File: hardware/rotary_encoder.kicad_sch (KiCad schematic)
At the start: 7 parts, among them U14 PEC11R-4215F-S0024

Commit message: Minor cosmetic changes
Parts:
- U14: footprint TO_215F-S0024 -> kitchen_timer:TO_215F-S0024
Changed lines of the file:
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@@
 			)
 		)
-		(property "Footprint" "TO_215F-S0024"
+		(property "Footprint" "kitchen_timer:TO_215F-S0024"
 			(at 102.108 72.39 0)
 			(effects

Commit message: Added information, footprints and 3d models for several components
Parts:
- U14: Package (none) -> Through_Hole; Part Num (none) -> PEC11R-4215F-S0024; Price/unit (none) -> $2.4720; Supplier Link (none) -> https://jlcpcb.com/partdetail/Bourns-PEC11R_4215FS0024/C143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
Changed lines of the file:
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@@
 			)
 		)
-		(property "Datasheet" "PEC11R-4215F-S0024"
+		(property "Datasheet" "https://www.lcsc.com/datasheet/lcsc_datasheet_2304140030_BOURNS-PEC11R-4215F-S0024_C143790.pdf"
 			(at 98.806 69.85 0)
 			(effects
@@
 			)
 		)
-		(property "Description" ""
+		(property "Description" "Plugin Rotary Encoders ROHS"
 			(at 123.19 73.66 90)
 			(effects
 				(font
+					(size 1.27 1.27)
+				)
+				(hide yes)
+			)
+		)
+		(property "Supplier Link" "https://jlcpcb.com/partdetail/Bourns-PEC11R_4215FS0024/C143790"
+			(at 124.46 80.01 0)
+			(effects
+				(font
+					(size 1.27 1.27)
+				)
+				(hide yes)
+			)
+		)
+		(property "Price/unit" "$2.4720"
+			(at 124.46 80.01 0)
+			(effects
+				(font
+					(size 1.27 1.27)
+				)
+				(hide yes)
+			)
+		)
+		(property "Part Num" "PEC11R-4215F-S0024"
+			(at 124.46 80.01 0)
+			(effects
+				(font
+					(size 1.27 1.27)
+				)
+				(hide yes)
+			)
+		)
+		(property "Package" "Through_Hole"
+			(at 124.46 80.01 0)
+			(effects
+				(font

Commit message: Added 3d models for footprints
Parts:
- U14: footprint kitchen_timer:TO_215F-S0024 -> kitchen_timer:PEC11R4215FS0024
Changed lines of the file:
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@@
 			)
 		)
-		(property "Footprint" "kitchen_timer:TO_215F-S0024"
+		(property "Footprint" "kitchen_timer:PEC11R4215FS0024"
 			(at 102.108 72.39 0)
 			(effects

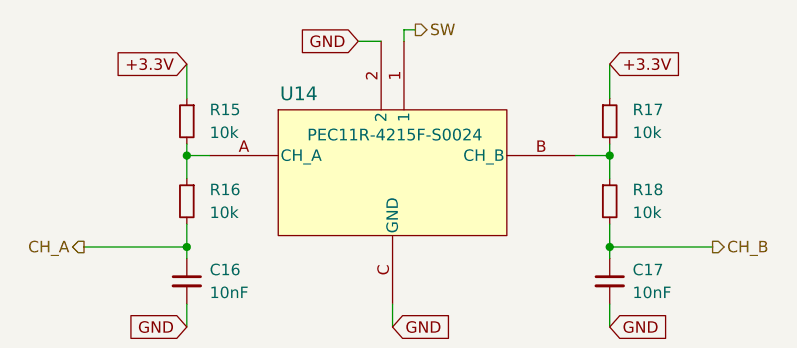
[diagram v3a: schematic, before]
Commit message: Removed the 3.3V Regulator since we might need to run everything out of 5V
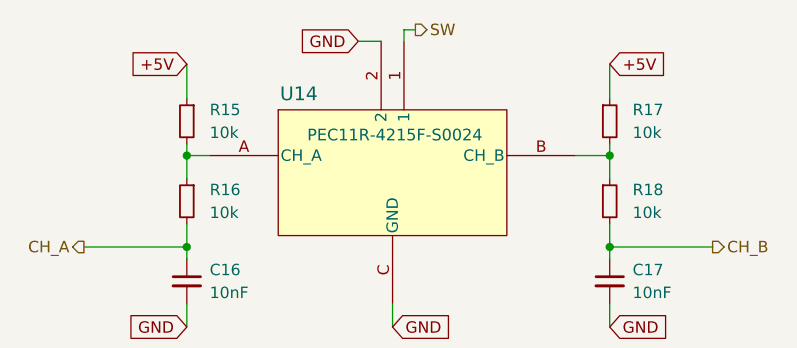
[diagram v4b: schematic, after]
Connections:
- net +3.3V renamed +5V
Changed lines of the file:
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@@
 		)
 	)
-	(global_label "+3.3V"
+	(global_label "+5V"
 		(shape input)
 		(at 101.6 68.58 180)
@@
 		)
 		(property "Intersheetrefs" "${INTERSHEET_REFS}"
-			(at 92.93 68.58 0)
+			(at 94.7443 68.58 0)
 			(effects
 				(font
@@
 		)
 	)
-	(global_label "+3.3V"
+	(global_label "+5V"
 		(shape input)
 		(at 148.59 68.58 0)
@@
 		)
 		(property "Intersheetrefs" "${INTERSHEET_REFS}"
-			(at 157.26 68.58 0)
+			(at 155.4457 68.58 0)
 			(effects
 				(font

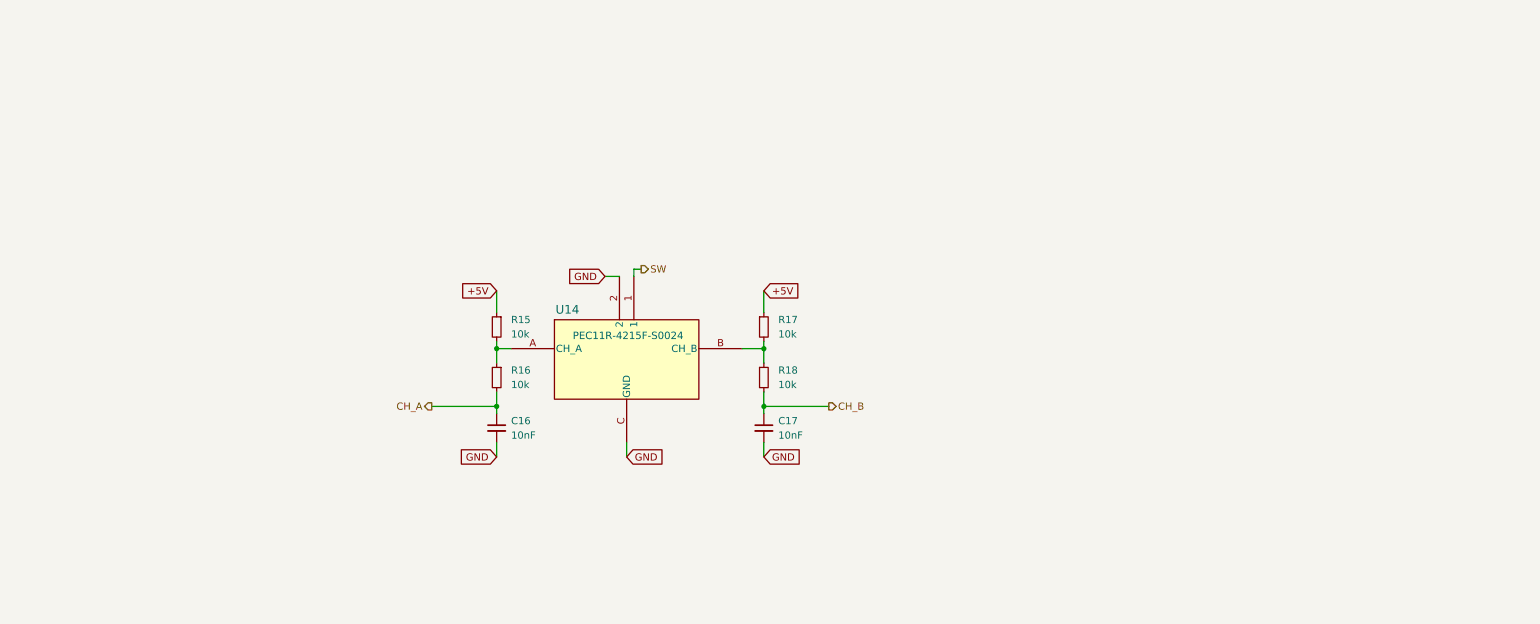
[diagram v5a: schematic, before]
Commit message: Schematic completed, commented and ready for review
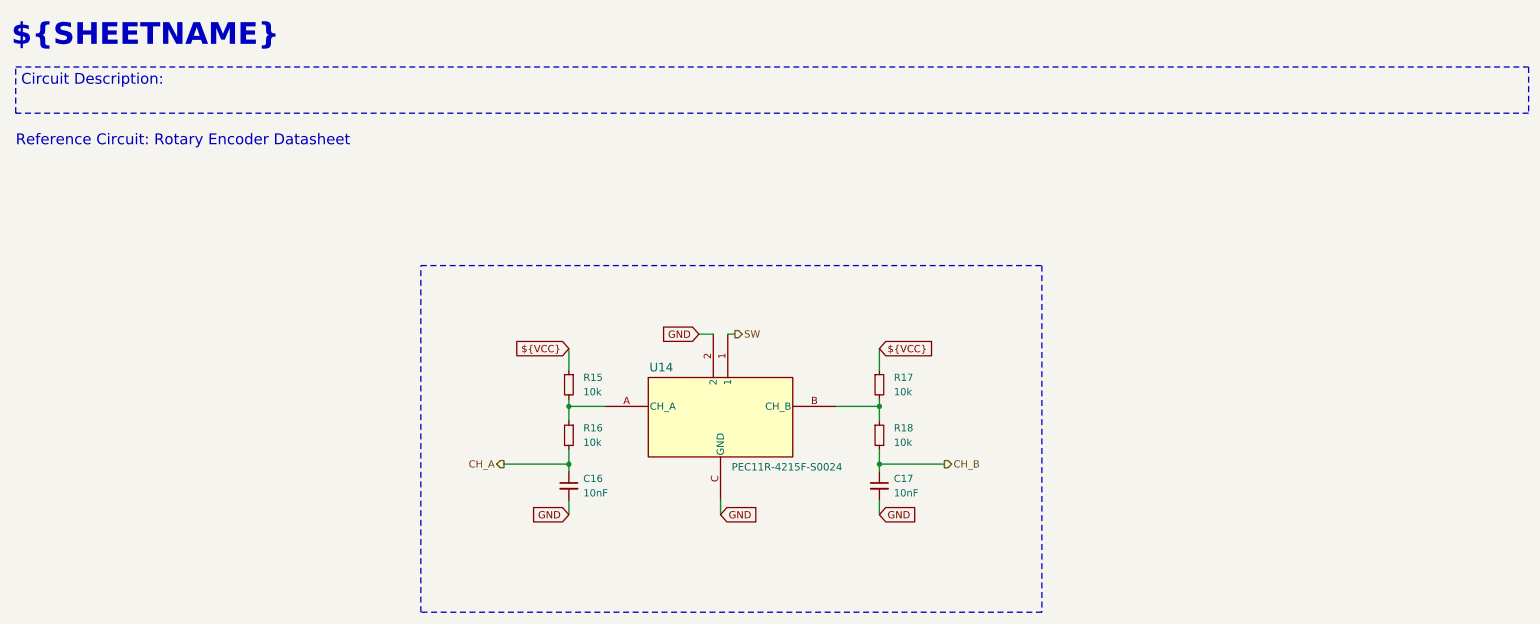
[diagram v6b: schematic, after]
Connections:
- net +5V renamed ${VCC}
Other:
- note added: "${SHEETNAME}"
- note added: "Reference Circuit: Rotary Encoder Datasheet"
- title: (none) -> Kitchen_Timer - ${SHEETNAME}
- moved on the sheet: C16, C17, R15, R16, R17, R18, U14

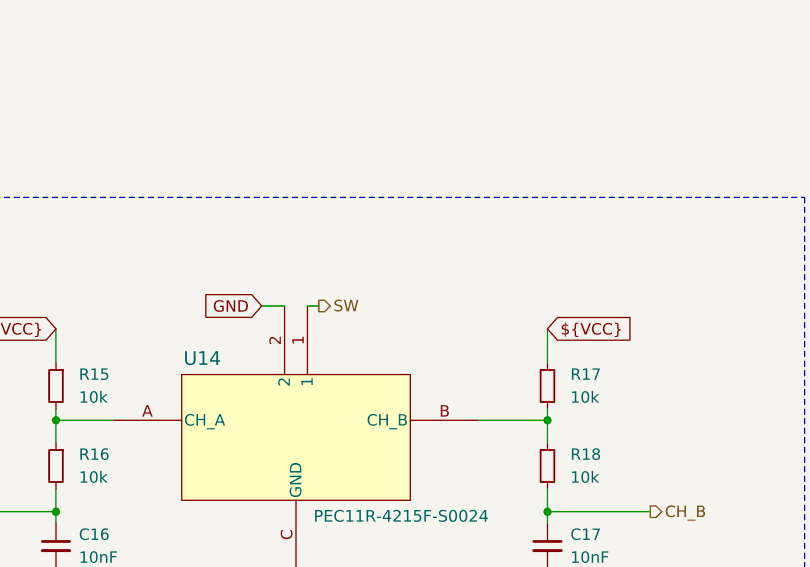
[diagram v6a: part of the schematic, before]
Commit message: Added filter to SW pin on Rotary Encoder
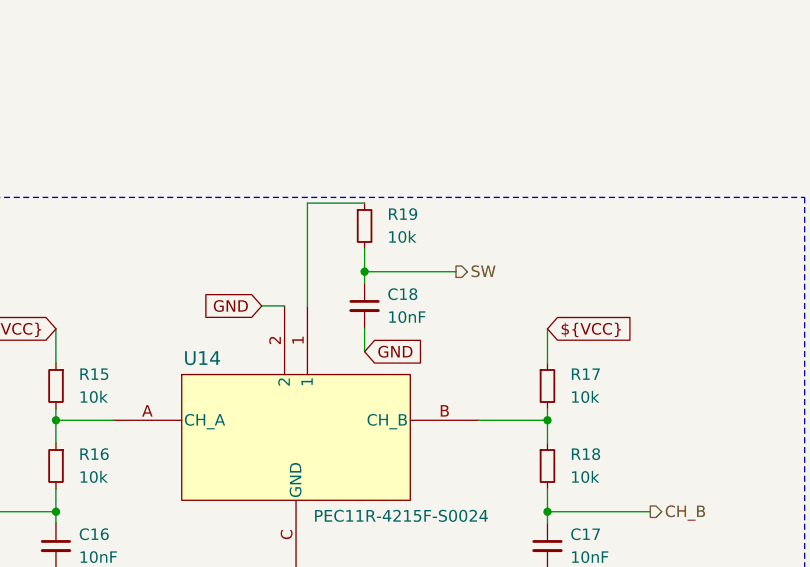
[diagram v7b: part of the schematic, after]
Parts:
- added C18: 10nF, symbol Device:C_Small
- added R19: 10k, symbol Device:R_Small
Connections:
- net GND: now also C18.2
- net SW: now also C18.1, R19.2; no longer U14.1
- new net: R19.1, U14.1
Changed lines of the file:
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@@
+	)
+	(junction
+		(at 148.59 72.39)
+		(diameter 0)
+		(color 0 0 0 0)
 	)
 	(junction
@@
 	(wire
 		(pts
-			(xy 143.51 76.2) (xy 142.24 76.2)
+			(xy 148.59 72.39) (xy 148.59 73.66)
 		)
 		(stroke
@@
 	(wire
 		(pts
+			(xy 148.59 72.39) (xy 158.75 72.39)
+		)
+		(stroke
+			(width 0)
+			(type default)
+		)
+	)
+	(wire
+		(pts
+			(xy 148.59 78.74) (xy 148.59 81.28)
+		)
+		(stroke
+			(width 0)
+			(type default)
+		)
+	)
+	(wire
+		(pts
 			(xy 114.3 88.9) (xy 114.3 87.63)
+		)
+		(stroke
+			(width 0)
+			(type default)
+		)
+	)
+	(wire
+		(pts
+			(xy 142.24 64.77) (xy 142.24 76.2)
+		)
+		(stroke
+			(width 0)
+			(type default)
+		)
+	)
+	(wire
+		(pts
+			(xy 142.24 64.77) (xy 148.59 64.77)
+		)
+		(stroke
+			(width 0)
+			(type default)
+		)
+	)
+	(wire
+		(pts
+			(xy 148.59 69.85) (xy 148.59 72.39)
 		)
 		(stroke
@@
 		)
 	)
+	(global_label "GND"
+		(shape input)
+		(at 148.59 81.28 0)
+		(fields_autoplaced yes)
+		(effects
+			(font
+				(size 1.27 1.27)
+			)
+			(justify left)
+		)
+		(property "Intersheetrefs" "${INTERSHEET_REFS}"
+			(at 155.4457 81.28 0)
+			(effects
+				(font
+					(size 1.27 1.27)
+				)
+				(justify left)
+				(hide yes)
+			)
+		)
+	)
 	(global_label "${VCC}"
 		(shape input)
@@
 	(hierarchical_label "SW"
 		(shape output)
-		(at 143.51 76.2 0)
+		(at 158.75 72.39 0)
 		(effects
 			(font
@@
 	(symbol
 		(lib_id "Device:R_Small")
+		(at 148.59 67.31 0)
+		(unit 1)
+		(exclude_from_sim no)
+		(in_bom yes)
+		(on_board yes)
+		(dnp no)
+		(fields_autoplaced yes)
+		(property "Reference" "R19"
+			(at 151.13 66.0399 0)
+			(effects
+				(font
+					(size 1.27 1.27)
+				)
+				(justify left)
+			)
+		)
+		(property "Value" "10k"
+			(at 151.13 68.5799 0)
+			(effects
+				(font
+					(size 1.27 1.27)
+				)
+				(justify left)
+			)
+		)
+		(property "Footprint" ""
+			(at 148.59 67.31 0)
+			(effects
+				(font
+					(size 1.27 1.27)
+				)
+				(hide yes)
+			)
+		)
+		(property "Datasheet" "~"
+			(at 148.59 67.31 0)
+			(effects
+				(font
+					(size 1.27 1.27)
+				)
+				(hide yes)
+			)
+		)
+		(property "Description" "Resistor, small symbol"
+			(at 148.59 67.31 0)
+			(effects
+				(font
+					(size 1.27 1.27)
+				)
+				(hide yes)
+			)
+		)
+		(pin "1"
+		)
+		(pin "2"
+		)
+		(instances
+			(project "kitchen_timer-hardware"
+				(path "/8963deea-96bc-4401-b671-98fbe9ed9c6a/0bd8e23b-f1a8-43a7-9e7f-c29366033bda"
+					(reference "R19")
+					(unit 1)
+				)
+			)
+		)
+	)
+	(symbol
+		(lib_id "Device:R_Small")
 		(at 114.3 85.09 0)
 		(mirror y)
@@
 					(unit 1)
 				)
+			)
+		)
+	)
+	(symbol
+		(lib_id "Device:C_Small")
+		(at 148.59 76.2 0)
+		(unit 1)
+		(exclude_from_sim no)
+		(in_bom yes)
+		(on_board yes)
+		(dnp no)
+		(fields_autoplaced yes)
+		(property "Reference" "C18"
+			(at 151.13 74.9362 0)
+			(effects
+				(font
+					(size 1.27 1.27)
+				)
+				(justify left)
+			)
+		)
+		(property "Value" "10nF"
+			(at 151.13 77.4762 0)
+			(effects
+				(font
+					(size 1.27 1.27)
+				)
+				(justify left)
+			)
+		)
+		(property "Footprint" ""
+			(at 148.59 76.2 0)
+			(effects
+				(font
+					(size 1.27 1.27)
+				)
+				(hide yes)
+			)
+		)
+		(property "Datasheet" "~"
+			(at 148.59 76.2 0)
+			(effects
+				(font
+					(size 1.27 1.27)
+				)
+				(hide yes)
+			)
+		)
+		(property "Description" "Unpolarized capacitor, small symbol"
+			(at 148.59 76.2 0)
+			(effects
+				(font
+					(size 1.27 1.27)
+				)
+				(hide yes)
+			)
+		)
+		(pin "1"
+		)
+		(pin "2"
+		)
+		(instances
+			(project "kitchen_timer-hardware"
+				(path "/8963deea-96bc-4401-b671-98fbe9ed9c6a/0bd8e23b-f1a8-43a7-9e7f-c29366033bda"
+					(reference "C18")
+					(unit 1)
+				)

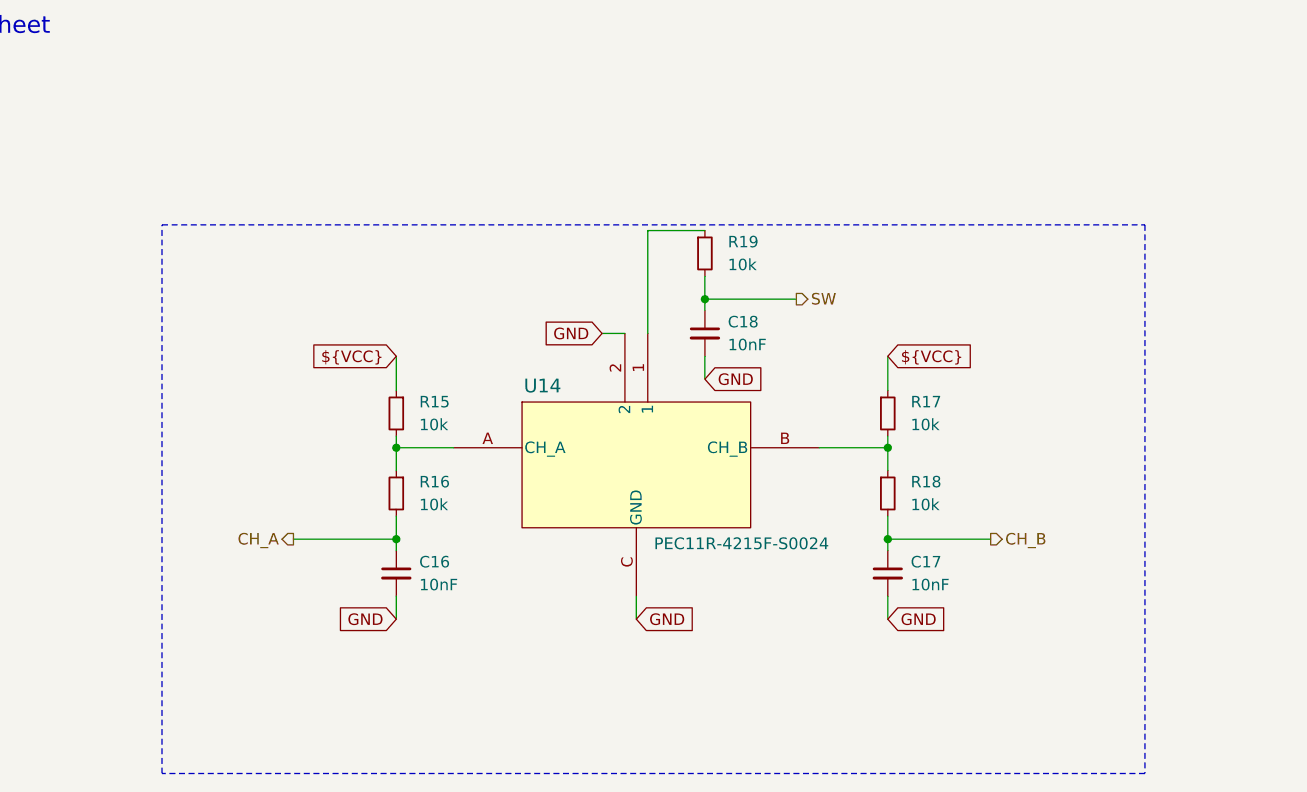
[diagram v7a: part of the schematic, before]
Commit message: Added comments to the TODO boxes after the meeting with Erasmus
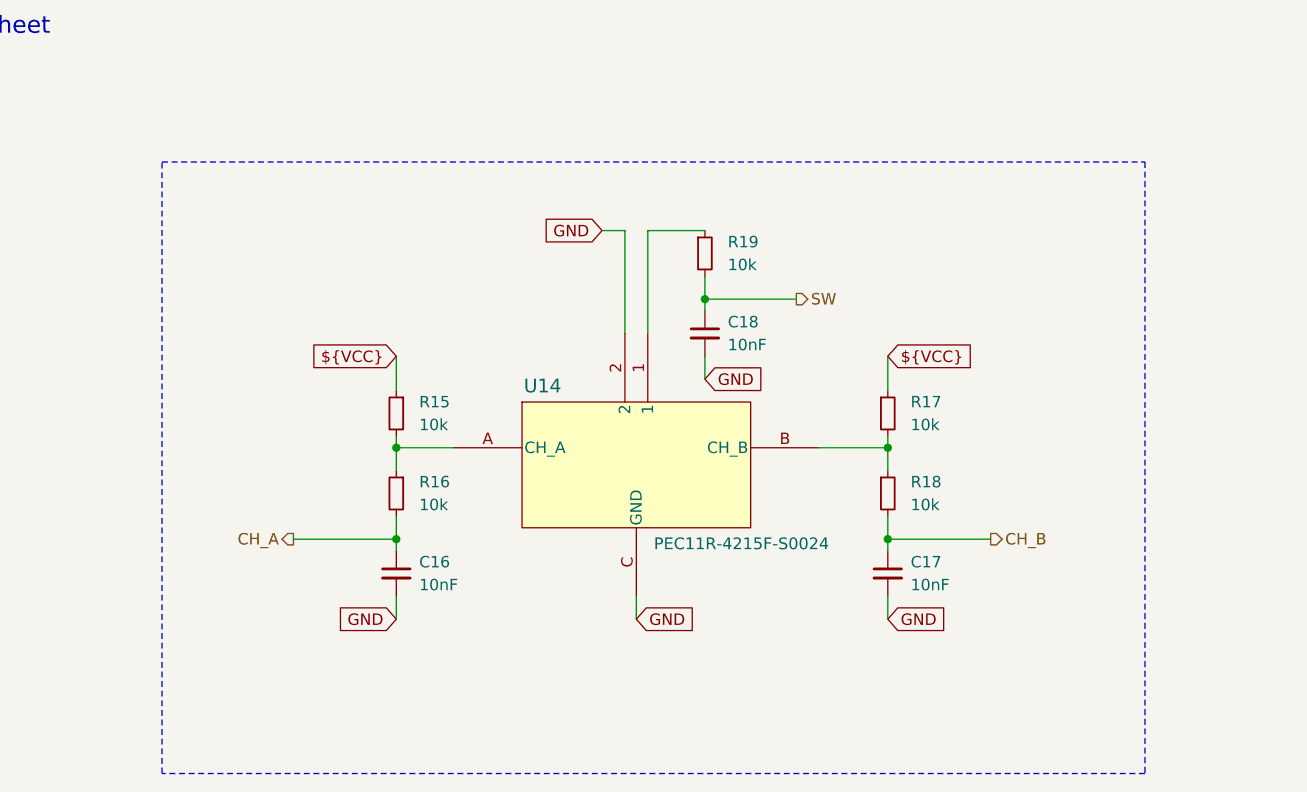
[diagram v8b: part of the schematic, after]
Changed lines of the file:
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@@
 	)
 	(rectangle
-		(start 88.265 64.135)
+		(start 88.265 57.15)
 		(end 197.485 125.095)
 		(stroke
@@
 	(wire
 		(pts
+			(xy 139.7 64.77) (xy 139.7 76.2)
+		)
+		(stroke
+			(width 0)
+			(type default)
+		)
+	)
+	(wire
+		(pts
 			(xy 168.91 96.52) (xy 168.91 99.06)
 		)
@@
 	(wire
 		(pts
-			(xy 137.16 76.2) (xy 139.7 76.2)
+			(xy 137.16 64.77) (xy 139.7 64.77)
 		)
 		(stroke
@@
 	(global_label "GND"
 		(shape input)
-		(at 137.16 76.2 180)
+		(at 137.16 64.77 180)
 		(fields_autoplaced yes)
 		(effects
@@
 		)
 		(property "Intersheetrefs" "${INTERSHEET_REFS}"
-			(at 130.3043 76.2 0)
+			(at 130.3043 64.77 0)
 			(effects
 				(font
